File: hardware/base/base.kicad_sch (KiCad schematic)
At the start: 69 parts, among them J1 SWD, J2 USB_B_Mini, J4 Serial Interface, J5 Debug, J5 OLED Display, J6 Conn_01x02_Pin, M1 Fan_ALT, Q1 Q_NMOS_GSD, Q2 Q_NMOS_GSD, Q3 Q_NMOS_GSD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

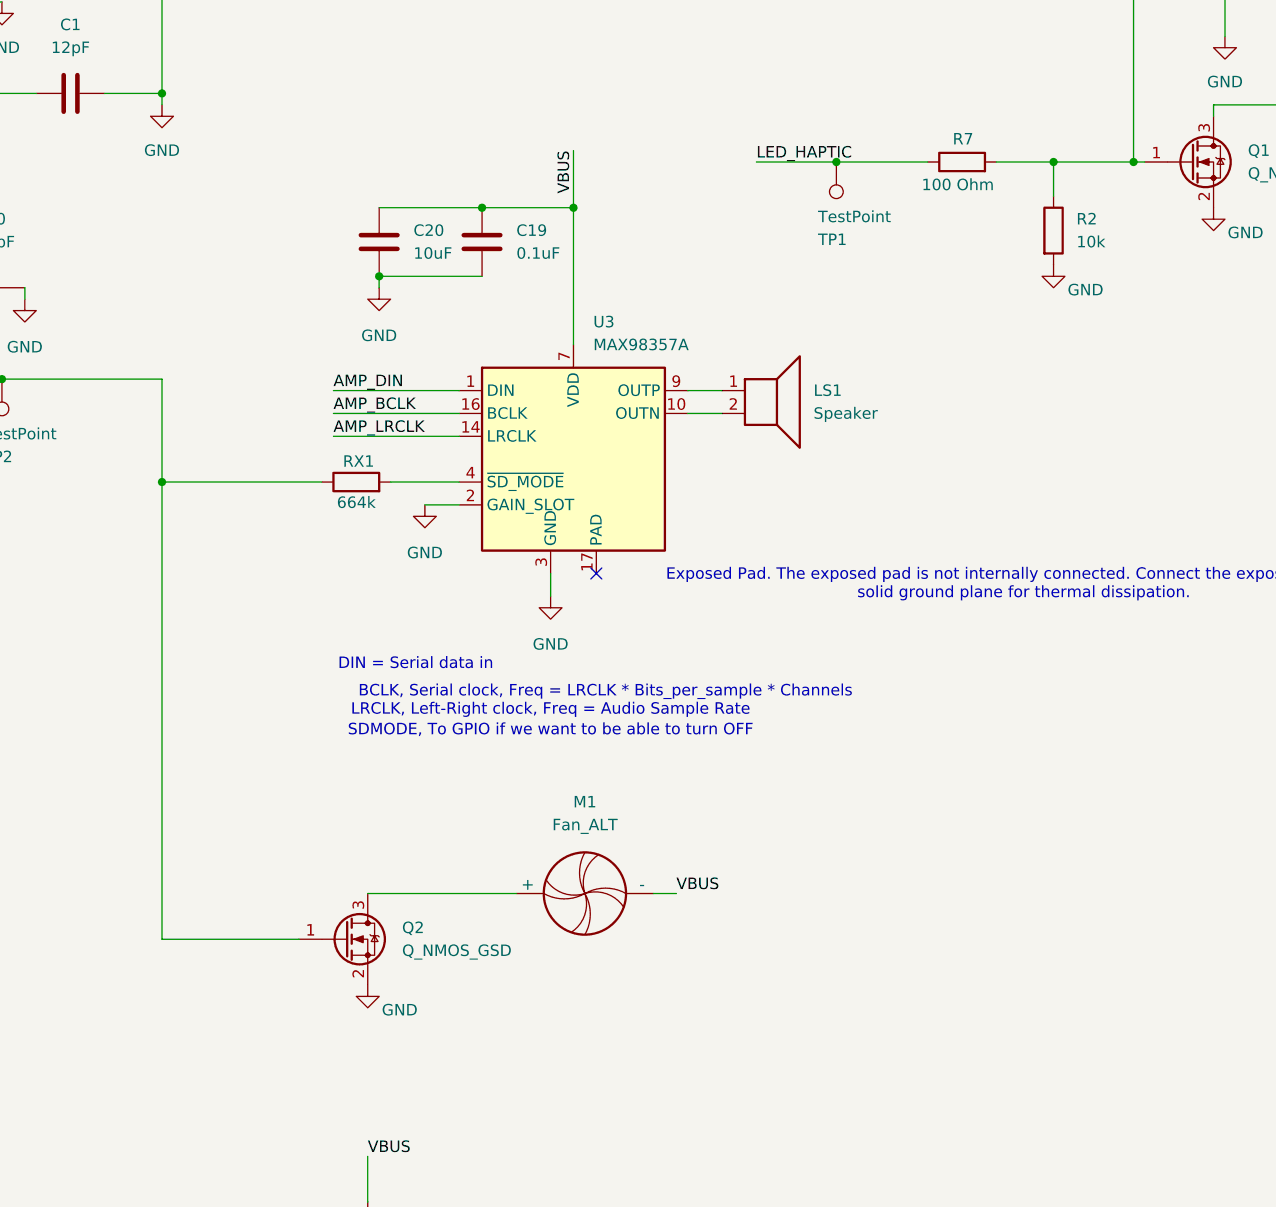
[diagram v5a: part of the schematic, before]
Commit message: update README, minor changes to schematic
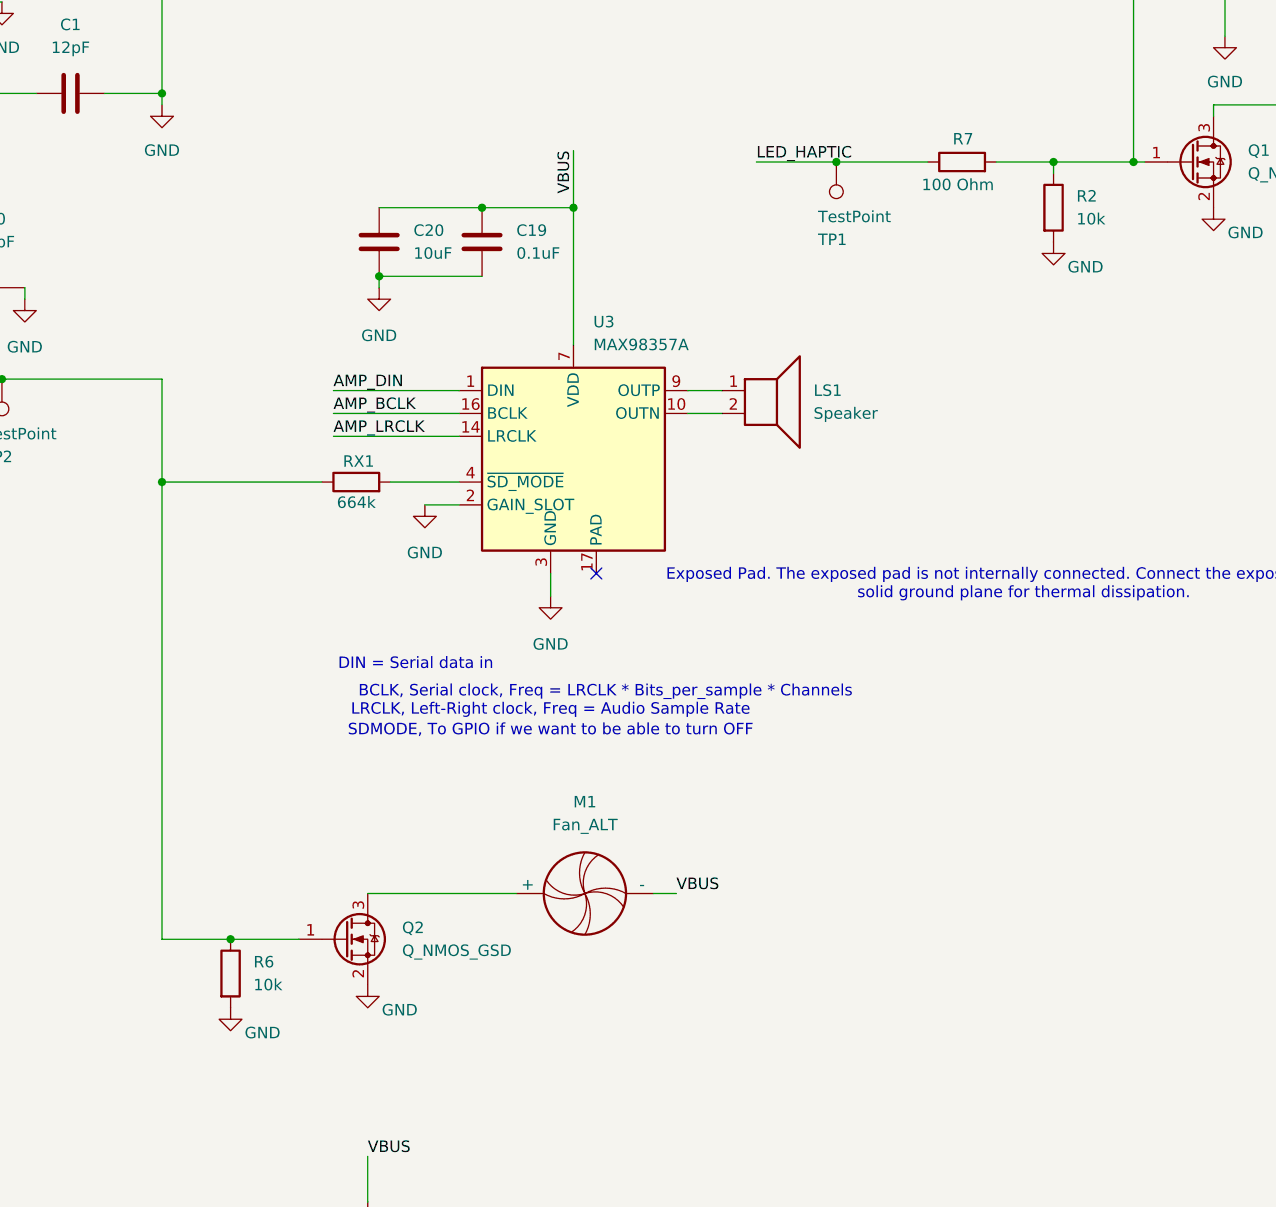
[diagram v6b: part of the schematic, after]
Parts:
- added R6: 10k, Resistor_SMD:R_0603_1608Metric, symbol Device:R
- BT1: footprint (none) -> 796136-1:TE_796136-1
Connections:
- net GND: now also R6.2
- net at Q2.1 (G), RX1.1, TP2.1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: now also R6.1
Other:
- moved on the sheet: R2
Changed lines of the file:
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@@
 	)
 	(junction
+		(at 232.41 168.91)
+		(diameter 0)
+		(color 0 0 0 0)
+	)
+	(junction
 		(at 270.51 87.63)
 		(diameter 0)
@@
 	(wire
 		(pts
+			(xy 232.41 168.91) (xy 240.03 168.91)
+		)
+		(stroke
+			(width 0)
+			(type default)
+		)
+	)
+	(wire
+		(pts
 			(xy 135.89 55.88) (xy 132.08 55.88)
 		)
@@
 	(wire
 		(pts
-			(xy 224.79 168.91) (xy 240.03 168.91)
+			(xy 224.79 168.91) (xy 232.41 168.91)
 		)
 		(stroke
@@
 	(wire
 		(pts
-			(xy 323.85 86.36) (xy 323.85 82.55)
+			(xy 323.85 83.82) (xy 323.85 82.55)
 		)
 		(stroke
@@
 	)
 	(symbol
+		(lib_id "Device:R")
+		(at 232.41 172.72 0)
+		(unit 1)
+		(exclude_from_sim no)
+		(in_bom yes)
+		(on_board yes)
+		(dnp no)
+		(fields_autoplaced yes)
+		(property "Reference" "R6"
+			(at 234.95 171.4499 0)
+			(effects
+				(font
+					(size 1.27 1.27)
+				)
+				(justify left)
+			)
+		)
+		(property "Value" "10k"
+			(at 234.95 173.9899 0)
+			(effects
+				(font
+					(size 1.27 1.27)
+				)
+				(justify left)
+			)
+		)
+		(property "Footprint" "Resistor_SMD:R_0603_1608Metric"
+			(at 230.632 172.72 90)
+			(effects
+				(font
+					(size 1.27 1.27)
+				)
+				(hide yes)
+			)
+		)
+		(property "Datasheet" "~"
+			(at 232.41 172.72 0)
+			(effects
+				(font
+					(size 1.27 1.27)
+				)
+				(hide yes)
+			)
+		)
+		(property "Description" "Resistor"
+			(at 232.41 172.72 0)
+			(effects
+				(font
+					(size 1.27 1.27)
+				)
+				(hide yes)
+			)
+		)
+		(pin "1"
+		)
+		(pin "2"
+		)
+		(instances
+			(project "base"
+				(path "/dfe856ae-b386-4d00-a01d-c584178519be"
+					(reference "R6")
+					(unit 1)
+				)
+			)
+		)
+	)
+	(symbol
 		(lib_id "Device:C")
 		(at 67.31 73.66 90)
@@
 	)
 	(symbol
+		(lib_id "power:GND")
+		(at 232.41 176.53 0)
+		(unit 1)
+		(exclude_from_sim no)
+		(in_bom yes)
+		(on_board yes)
+		(dnp no)
+		(property "Reference" "#PWR011"
+			(at 232.41 182.88 0)
+			(effects
+				(font
+					(size 1.27 1.27)
+				)
+				(hide yes)
+			)
+		)
+		(property "Value" "GND"
+			(at 235.966 179.324 0)
+			(effects
+				(font
+					(size 1.27 1.27)
+				)
+			)
+		)
+		(property "Footprint" ""
+			(at 232.41 176.53 0)
+			(effects
+				(font
+					(size 1.27 1.27)
+				)
+				(hide yes)
+			)
+		)
+		(property "Datasheet" ""
+			(at 232.41 176.53 0)
+			(effects
+				(font
+					(size 1.27 1.27)
+				)
+				(hide yes)
+			)
+		)
+		(property "Description" "Power symbol creates a global label with name \"GND\" , ground"
+			(at 232.41 176.53 0)
+			(effects
+				(font
+					(size 1.27 1.27)
+				)
+				(hide yes)
+			)
+		)
+		(pin "1"
+		)
+		(instances
+			(project "base"
+				(path "/dfe856ae-b386-4d00-a01d-c584178519be"
+					(reference "#PWR011")
+					(unit 1)
+				)
+			)
+		)
+	)
+	(symbol
 		(lib_id "Connector:Conn_01x02_Pin")
 		(at 278.13 237.49 180)
@@
 			)
 		)
-		(property "Footprint" ""
+		(property "Footprint" "796136-1:TE_796136-1"
 			(at 78.74 239.776 90)
 			(effects
@@
 	(symbol
 		(lib_id "power:GND")
-		(at 323.85 93.98 0)
+		(at 323.85 91.44 0)
 		(unit 1)
 		(exclude_from_sim no)
@@
 		(dnp no)
 		(property "Reference" "#PWR08"
-			(at 323.85 100.33 0)
+			(at 323.85 97.79 0)
 			(effects
 				(font
@@
 		)
 		(property "Value" "GND"
-			(at 327.406 96.774 0)
+			(at 327.406 94.234 0)
 			(effects
 				(font
@@
 		)
 		(property "Footprint" ""
-			(at 323.85 93.98 0)
+			(at 323.85 91.44 0)
 			(effects
 				(font
@@
 		)
 		(property "Datasheet" ""
-			(at 323.85 93.98 0)
+			(at 323.85 91.44 0)
 			(effects
 				(font
@@
 		)
 		(property "Description" "Power symbol creates a global label with name \"GND\" , ground"
-			(at 323.85 93.98 0)
+			(at 323.85 91.44 0)
 			(effects
 				(font
@@
 	(symbol
 		(lib_id "Device:R")
-		(at 323.85 90.17 0)
+		(at 323.85 87.63 0)
 		(unit 1)
 		(exclude_from_sim no)
@@
 		(fields_autoplaced yes)
 		(property "Reference" "R2"
-			(at 326.39 88.8999 0)
+			(at 326.39 86.3599 0)
 			(effects
 				(font
@@
 		)
 		(property "Value" "10k"
-			(at 326.39 91.4399 0)
+			(at 326.39 88.8999 0)
 			(effects
 				(font
@@
 		)
 		(property "Footprint" "Resistor_SMD:R_0603_1608Metric"
-			(at 322.072 90.17 90)
+			(at 322.072 87.63 90)
 			(effects
 				(font
@@
 		)
 		(property "Datasheet" "~"
-			(at 323.85 90.17 0)
+			(at 323.85 87.63 0)
 			(effects
 				(font
@@
 		)
 		(property "Description" "Resistor"
-			(at 323.85 90.17 0)
+			(at 323.85 87.63 0)
 			(effects
 				(font

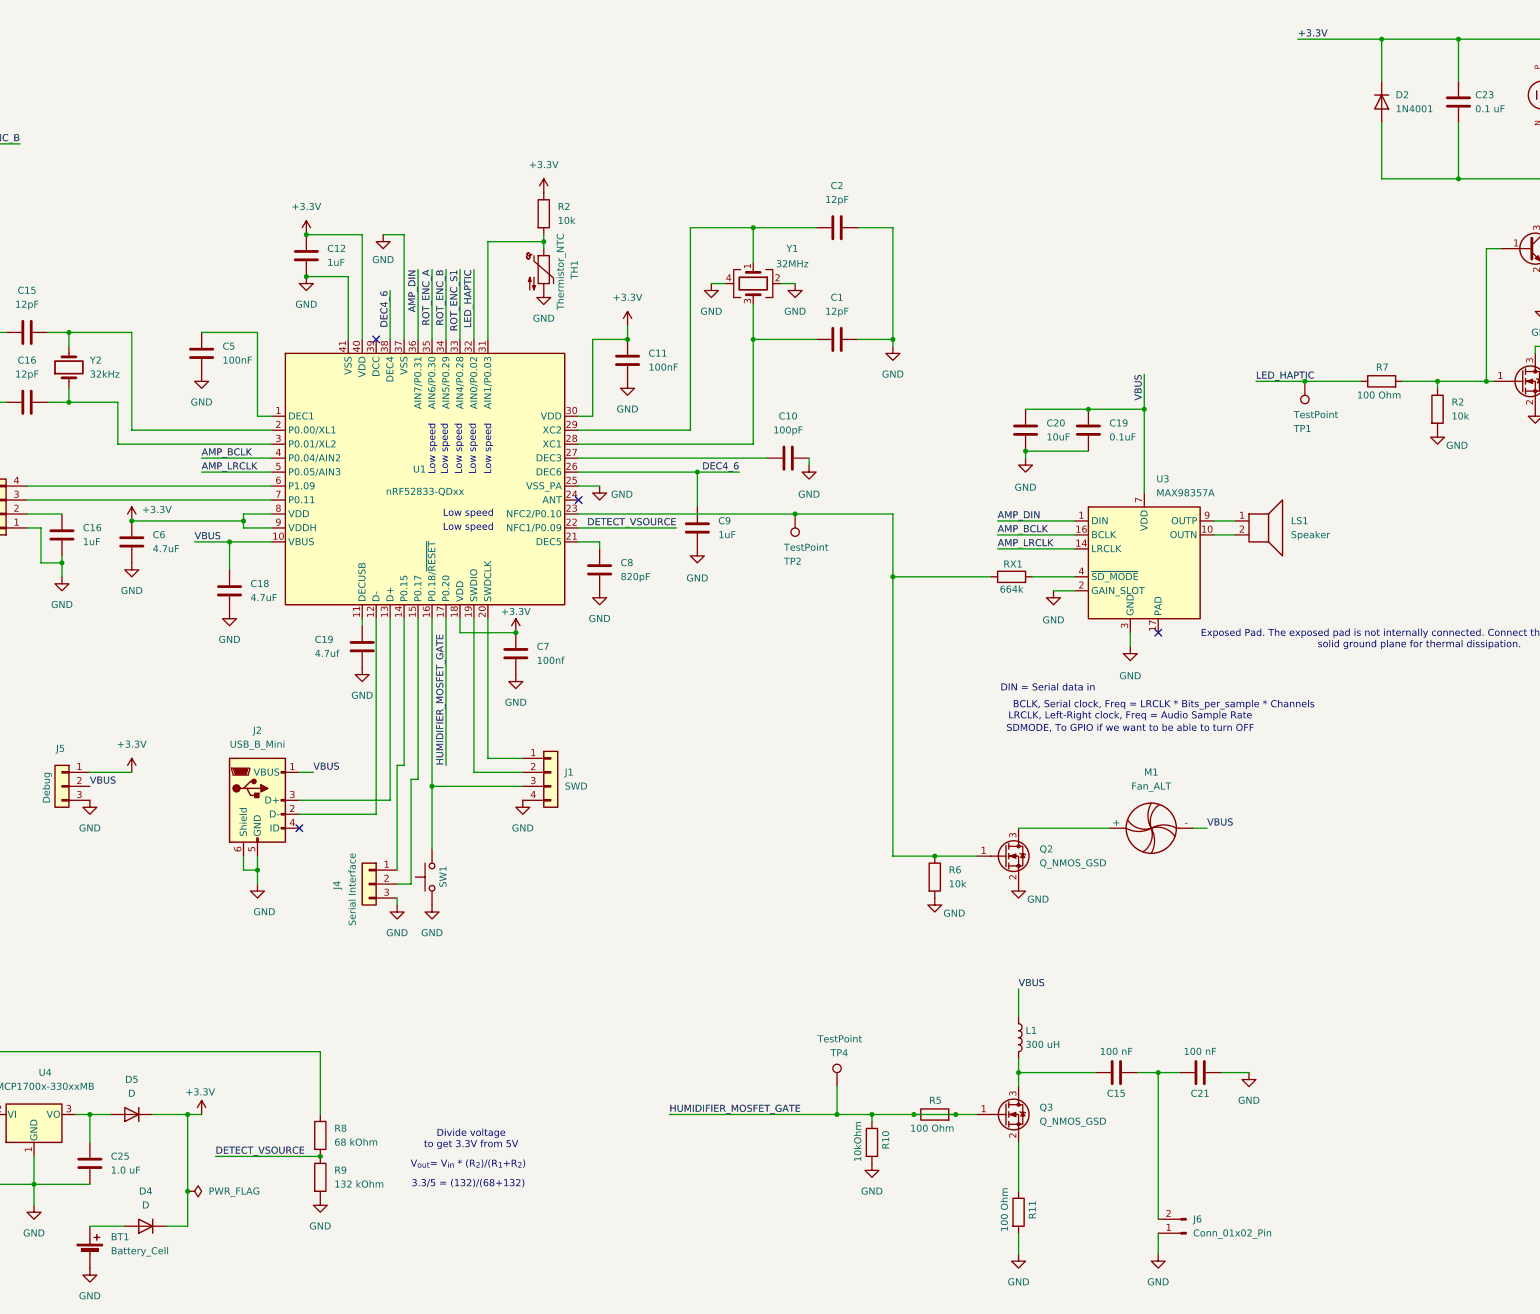
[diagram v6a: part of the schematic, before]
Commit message: import components to PCB
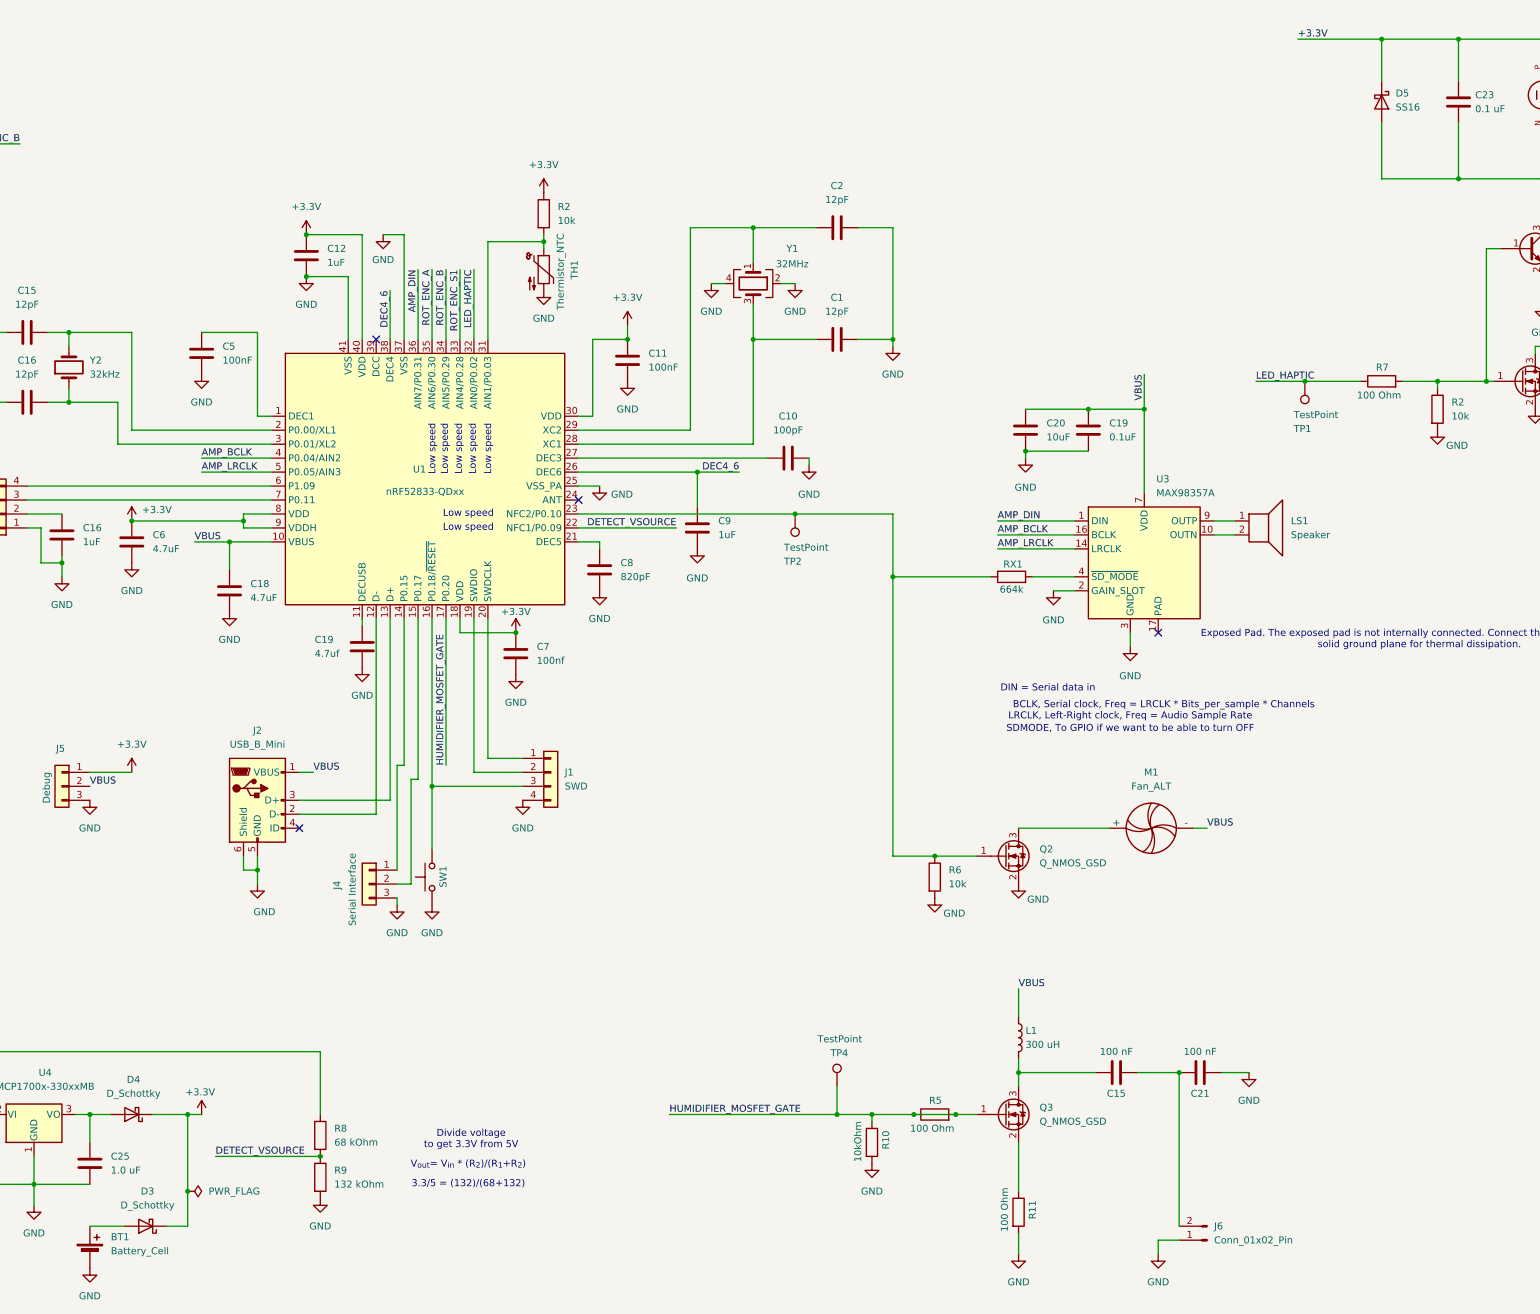
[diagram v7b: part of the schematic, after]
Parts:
- removed D2: 1N4001, Diode_THT:D_DO-41_SOD81_P10.16mm_Horizontal, symbol Diode:1N4001
- removed D4, D5: D, symbol Device:D
- added D3, D4: D_Schottky, Diode_SMD:D_MiniMELF, symbol Device:D_Schottky
- added D5: SS16, Schottky Rectifier (SS16):DIOM4325X250N, symbol Diode:SS16
- B1: footprint HD-EMC1203-LW20-R:PUI_HD-EMC1203-LW20-R -> Connector_PinHeader_2.54mm:PinHeader_1x02_P2.54mm_Vertical
- BT1: footprint 796136-1:TE_796136-1 -> Battery Holder (796136-1):TE_796136-1
- J6, LS1: footprint (none) -> Connector_PinHeader_2.54mm:PinHeader_1x02_P2.54mm_Vertical
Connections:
- net +3.3V: now also D3.1 (K), D4.1 (K), D5.1 (K)
- net at C25.1, U4.3 (VO): now also D4.2 (A)
- net at B1.N, C23.2, Q4.3 (C): now also D5.2 (A)
- net at BT1.1 (+): now also D3.2 (A)
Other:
- moved on the sheet: J6
